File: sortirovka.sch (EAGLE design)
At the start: 40 parts, among them IC1 DS1307/PCF8583, U1 MAX3485CSA, X1 PI3-CONMINIBOARD, X10 MKDSN1,5/3-5,08, X3 MKDSN1,5/4-5,08, X4 MKDSN1,5/2-5,08, X6 22-23-2051

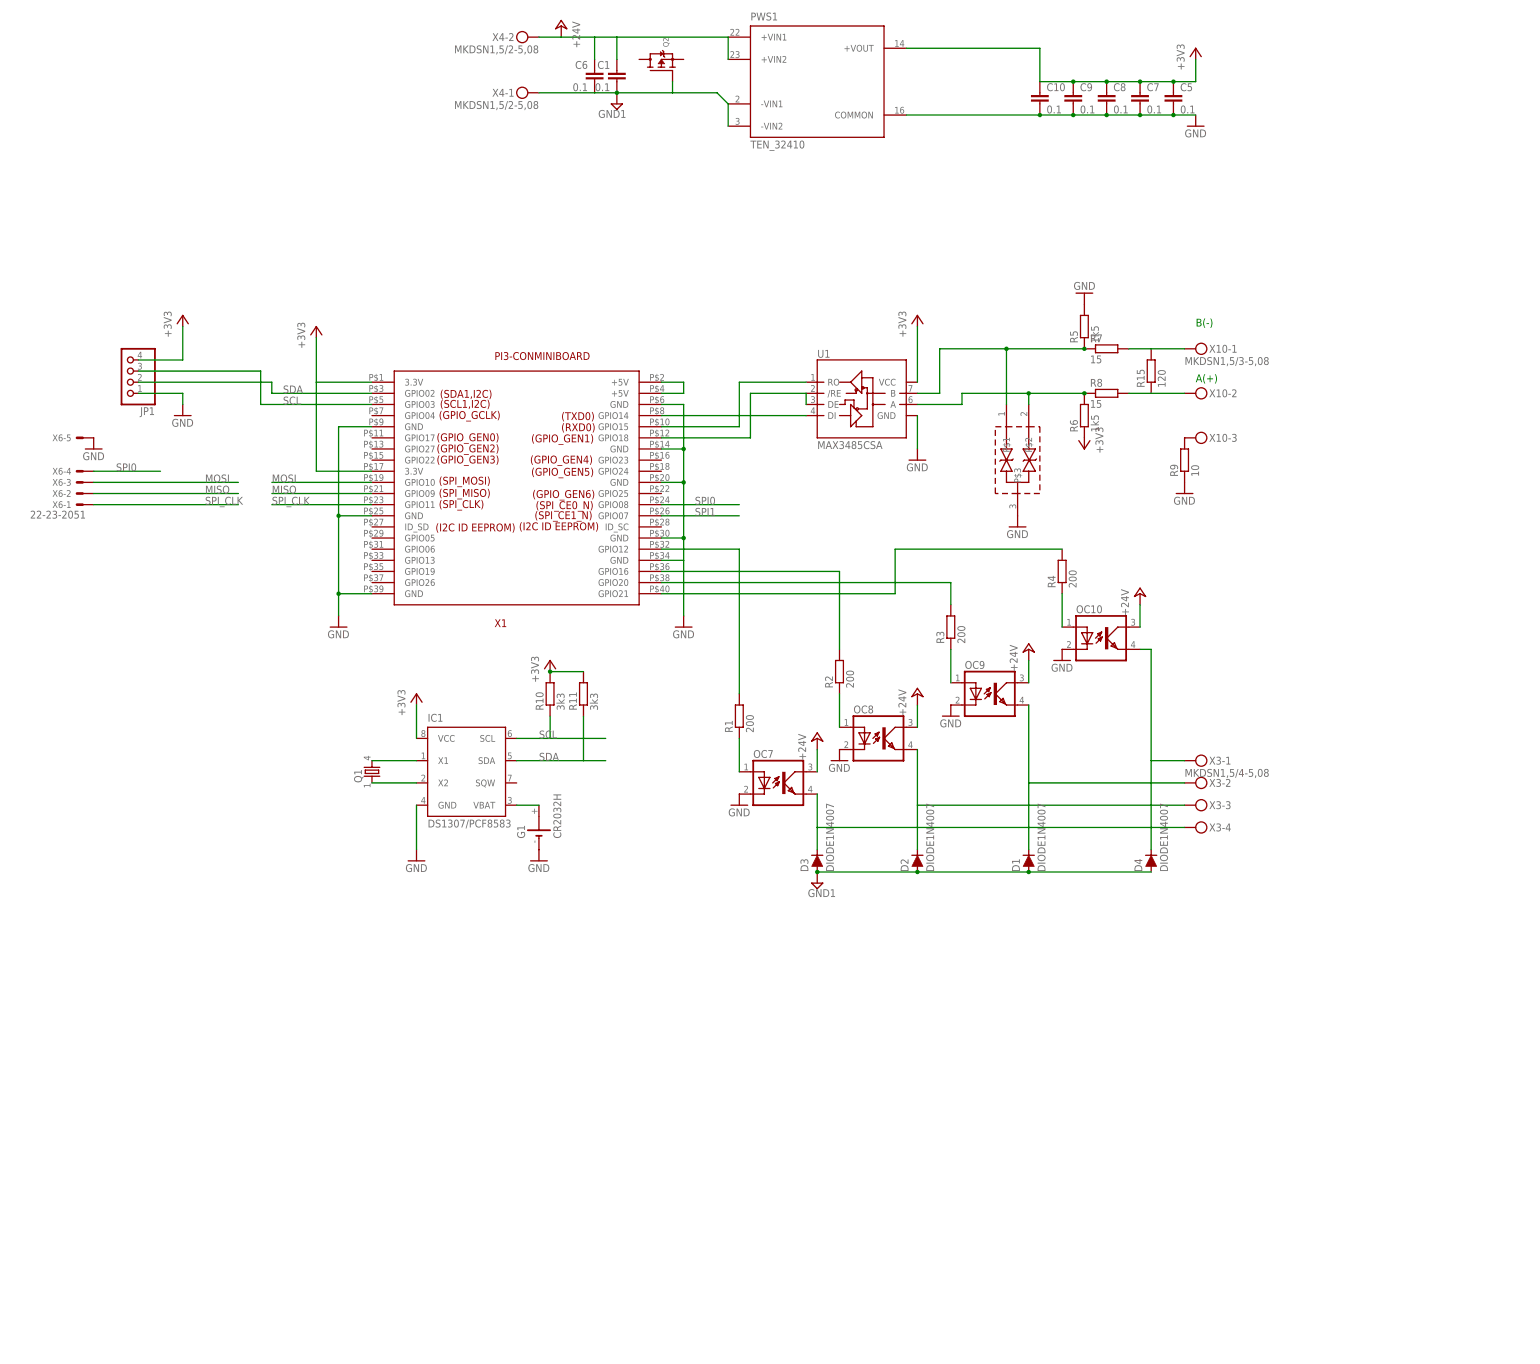
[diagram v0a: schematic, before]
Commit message: could be produced
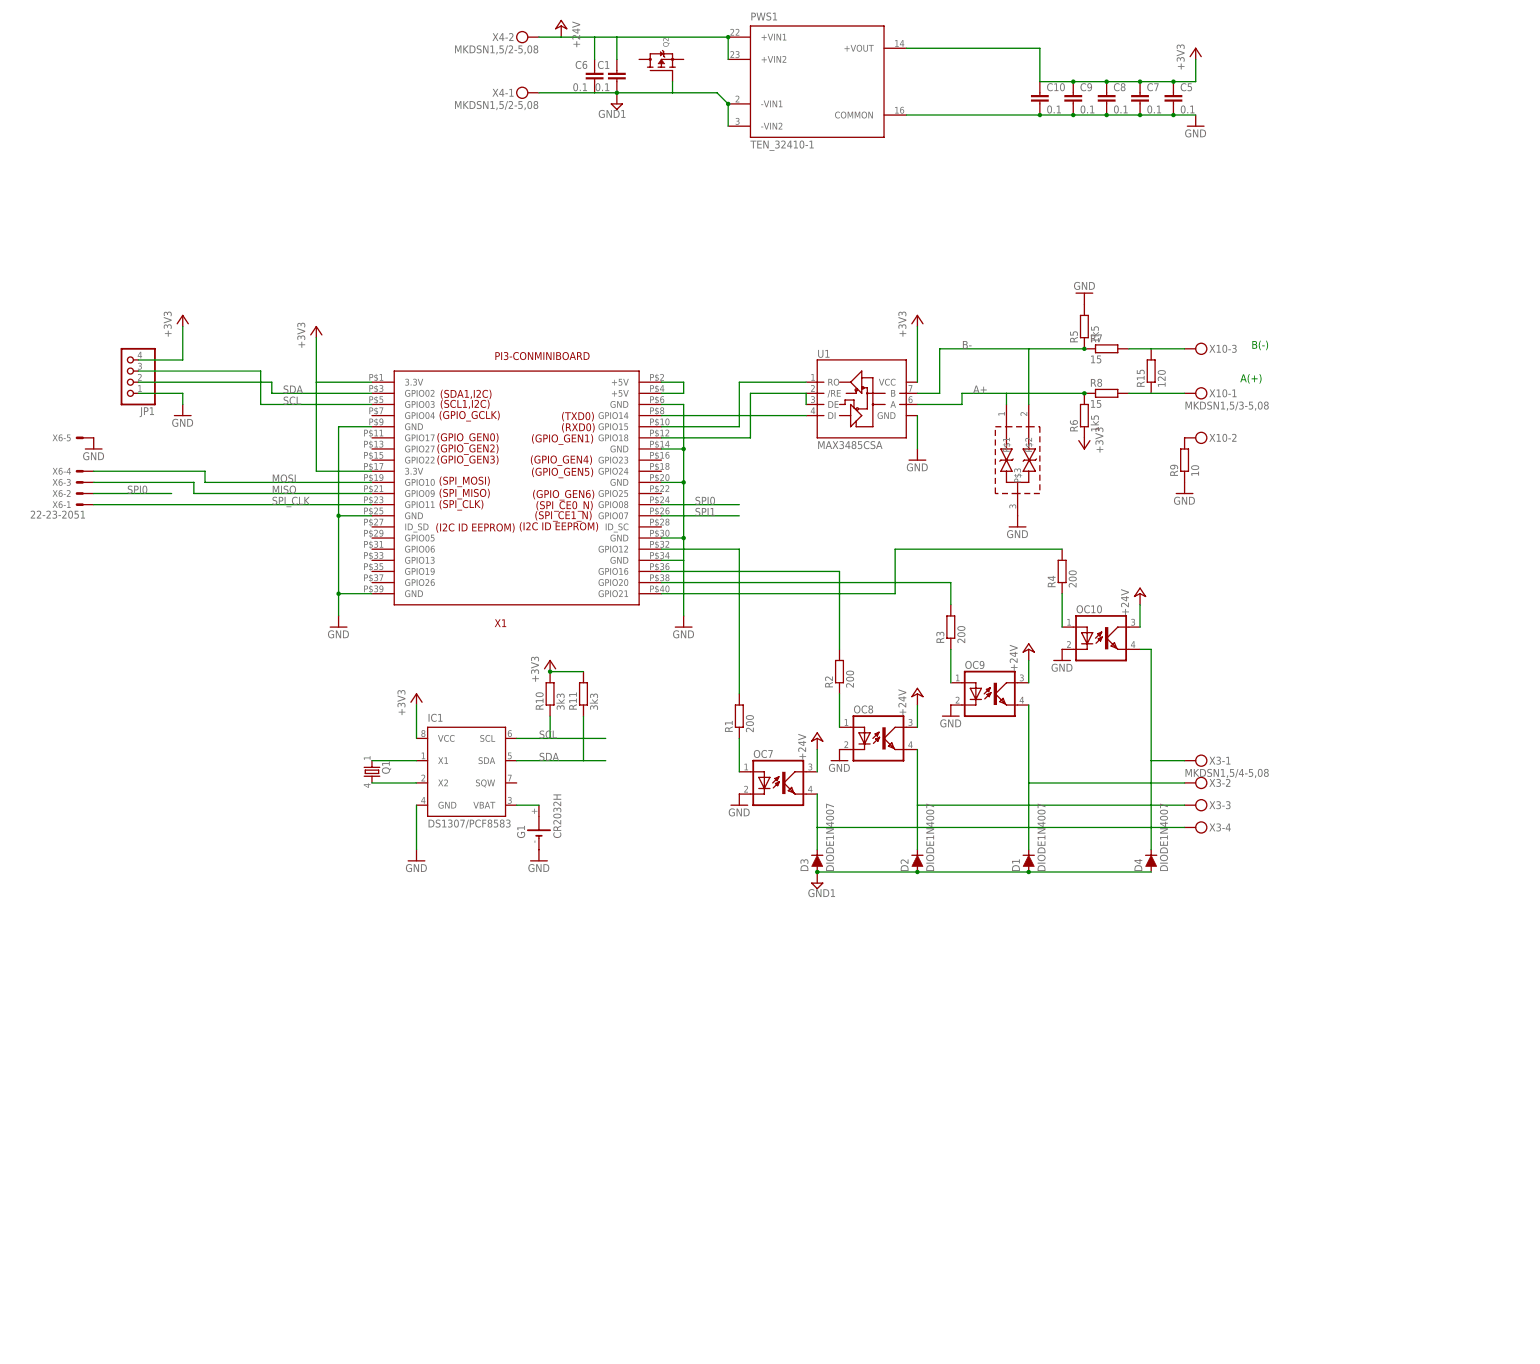
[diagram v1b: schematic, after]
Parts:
- PWS1: value TEN_32410 -> TEN_32410-1; device traco-electronic:TEN_32410 -> MyLib:TEN_32410-1
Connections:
- removed net N$47: R6.2, R8.1, U$3.P$2, U1.A
- removed net N$9: IC1.X2, Q1.1
- new net A+: R6.2, R8.1, U$3.P$1, U1.A
- new net B-: R5.1, R7.1, U$3.P$2, U1.B
- net MISO: now also X6-3.S; no longer X6-2.S
- net MOSI: now also X6-4.S; no longer X6-3.S
- net N$4: now also IC1.X1, Q1.1; no longer R5.1, R7.1, U$3.P$1, U1.B
- net N$45: now also X10-3.KL; no longer X10-1.KL
- net N$46: now also X10-1.KL; no longer X10-2.KL
- net N$5: now also X10-2.KL; no longer X10-3.KL
- net N$8: now also IC1.X2; no longer IC1.X1
- net SPI0: now also X6-2.S; no longer X6-4.S
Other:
- moved on the sheet: Q1, X10-1, X10-2, X10-3

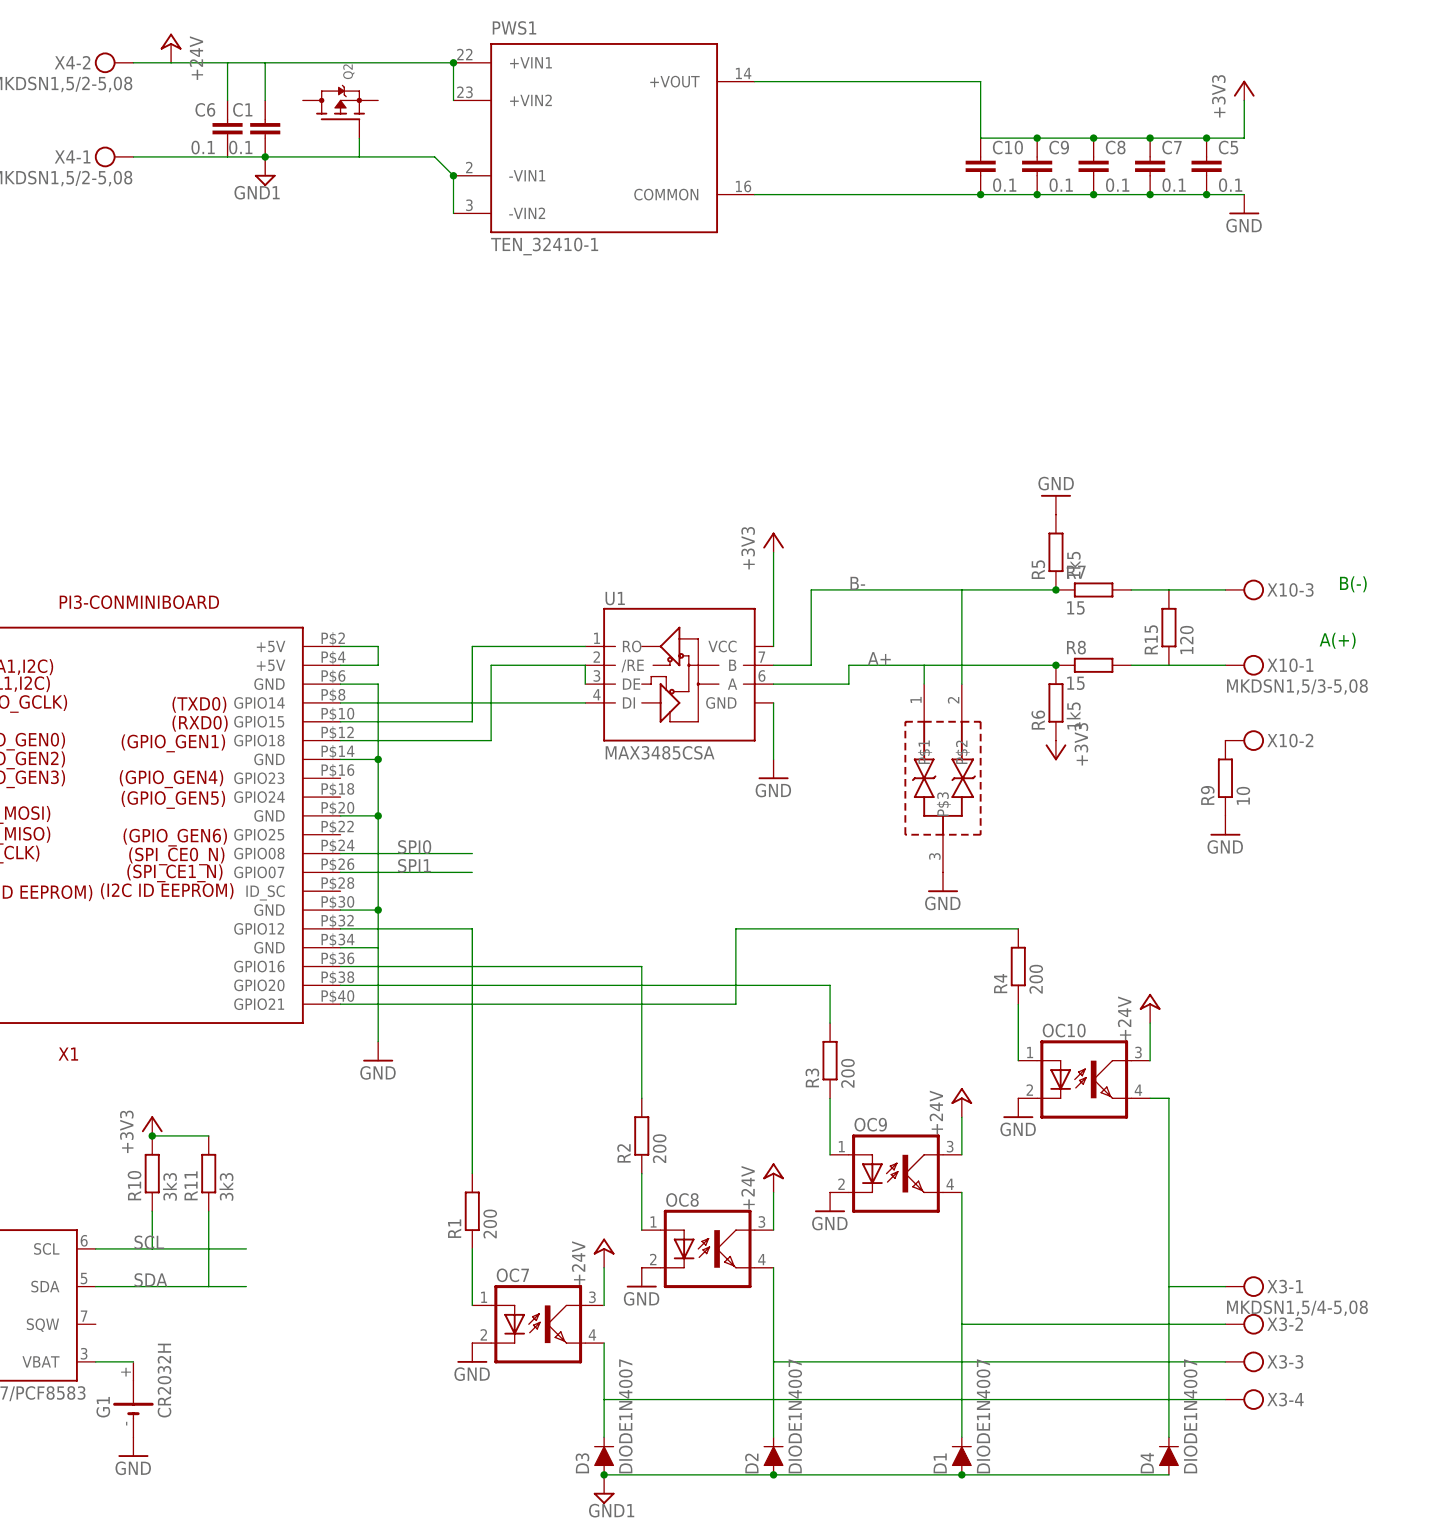
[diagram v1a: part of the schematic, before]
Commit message: not diode - supreesor
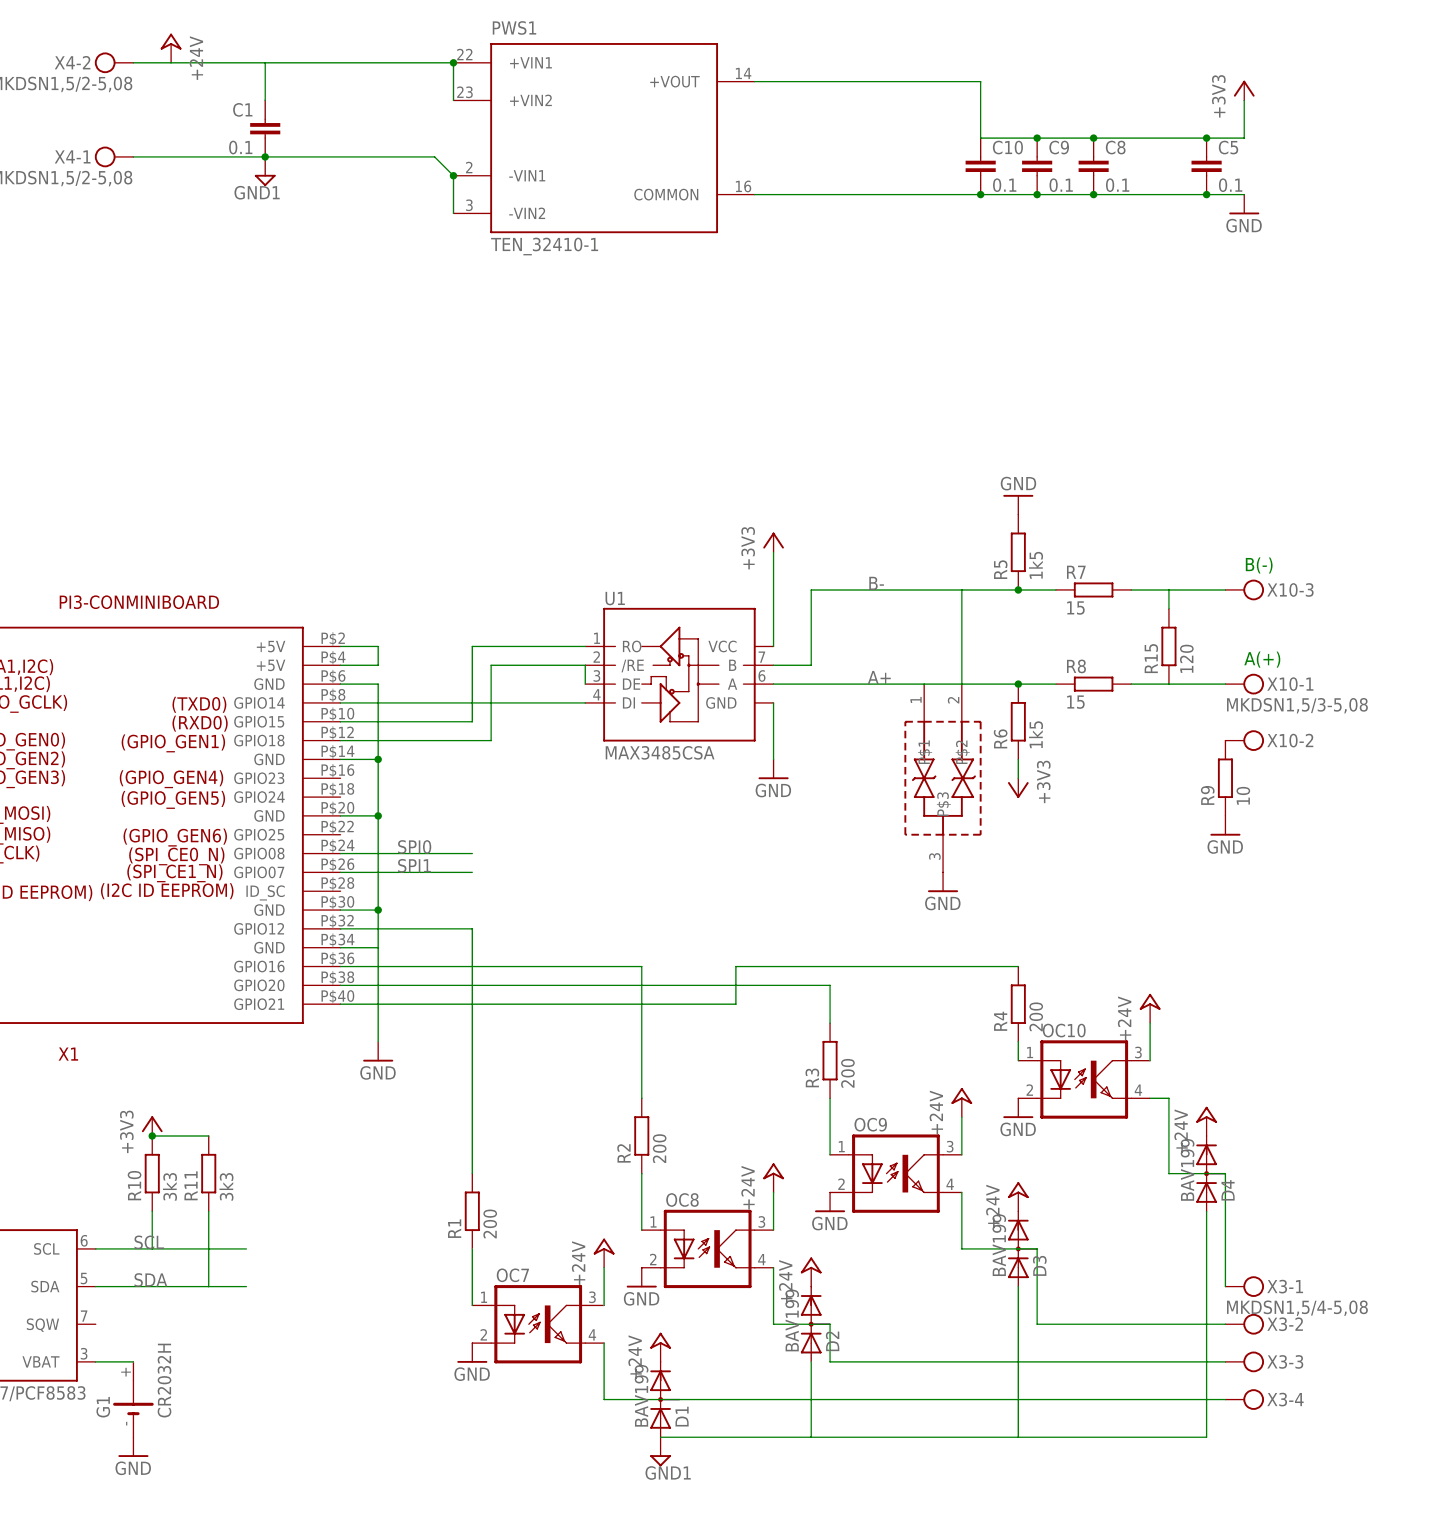
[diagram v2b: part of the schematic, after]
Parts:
- removed C6, C7: 0.1, rcl:C-EUC0805
- removed Q2: (no value), MyLib:IRLMS6702PBF
- D1, D2, D3, D4: value DIODE1N4007 -> BAV199; device MyLib:DIODE1N4007 -> MyLib:BAV199
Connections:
- removed net N$13 (its old number): D3.C, OC7.EMIT, X3-4.KL
- removed net N$14: Q2.D@1, Q2.D@2, Q2.D@3, Q2.D@4
- new net N$9: D1.AC, OC7.EMIT, X3-4.KL
- net +24V: now also D1.C, D2.C, D3.C, D4.C; no longer C6.1
- net +3V3: no longer C7.1
- net GND: no longer C7.2
- net GND1: no longer C6.2, Q2.G
- net N$10: now also D4.AC; no longer D4.C
- net N$11: now also D3.AC; no longer D1.C
- net N$12: now also D2.AC; no longer D2.C
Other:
- moved on the sheet: R15, R4, R5, R6, R8, X10-1

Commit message: wip
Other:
- moved on the sheet: D1, D2, D3, D4, OC10, OC7, OC8, OC9, R1, R2, R3, R4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
